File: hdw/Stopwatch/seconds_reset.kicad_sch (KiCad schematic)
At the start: 9 parts

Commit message: added more reset stuff
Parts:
- added C? (x4): 0.1uF, Capacitors_SMD:C_0603, symbol Custom_Library:C_Custom
- added R? (x4): 10k, Resistors_SMD:R_0603, symbol Custom_Library:R_Custom
- added U?: 74LVC1G97, Package_TO_SOT_SMD:SOT-363_SC-70-6, symbol Custom Library:74LVC1G97_Power_OR
- added U? (x3): 74LVC1G97, Package_TO_SOT_SMD:SOT-363_SC-70-6, symbol Custom Library:74LVC1G97_Power_AND
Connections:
- net +3.3V: now also U?.3 (VCC), U?.5 (VCC), U?.5 (VCC), U?.5 (VCC), U?.5 (VCC)
- net +3V3: now also C?.1, C?.1, C?.1, C?.1
- net GND: now also C?.2, C?.2, C?.2, C?.2, R?.2, R?.2, R?.2, R?.2, U?.1 (GND), U?.1 (GND), U?.1 (GND), U?.2 (GND), U?.2 (GND), U?.2 (GND), U?.2 (GND)
- net Stage01_SEG_G: now also U?.3
- net at R?.1, U?.4: now also U?.3
- net at R?.1, U?.4: now also U?.6 (x2)
- new net: R?.1, U?.4, U?.6 (x2)
- new net: R?.1, U?.3, U?.4
- new net Count_Reset: U?.1
- new net Seconds_Reset: R?.1, U?.4

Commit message: added some more junk
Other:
- company: (none) -> Drew Maatman
- title: (none) -> Stopwatch
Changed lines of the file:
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@@
 (kicad_sch (version 20230121) (generator eeschema)
   (paper "A")
+  (title_block
+    (title "Stopwatch")
+    (date "2024-01-11")
+    (rev "A")
+    (company "Drew Maatman")
+  )
   (junction (at 223.52 39.37) (diameter 0) (color 0 0 0 0)
   )

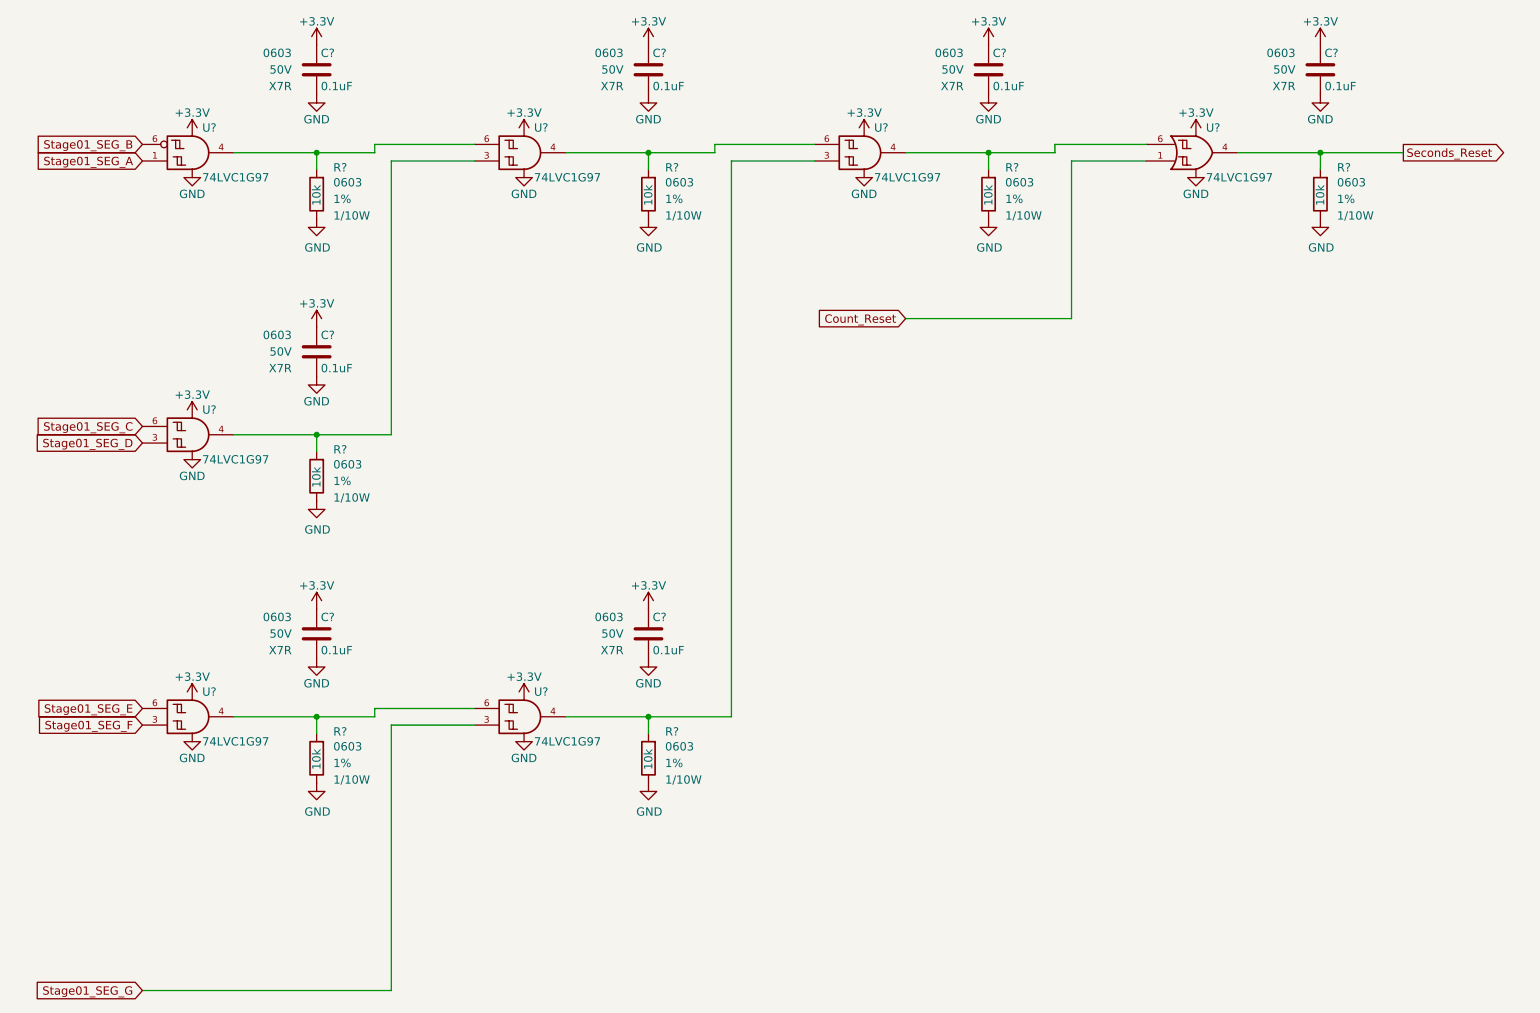
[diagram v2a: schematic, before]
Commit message: Assigned some digikey pns
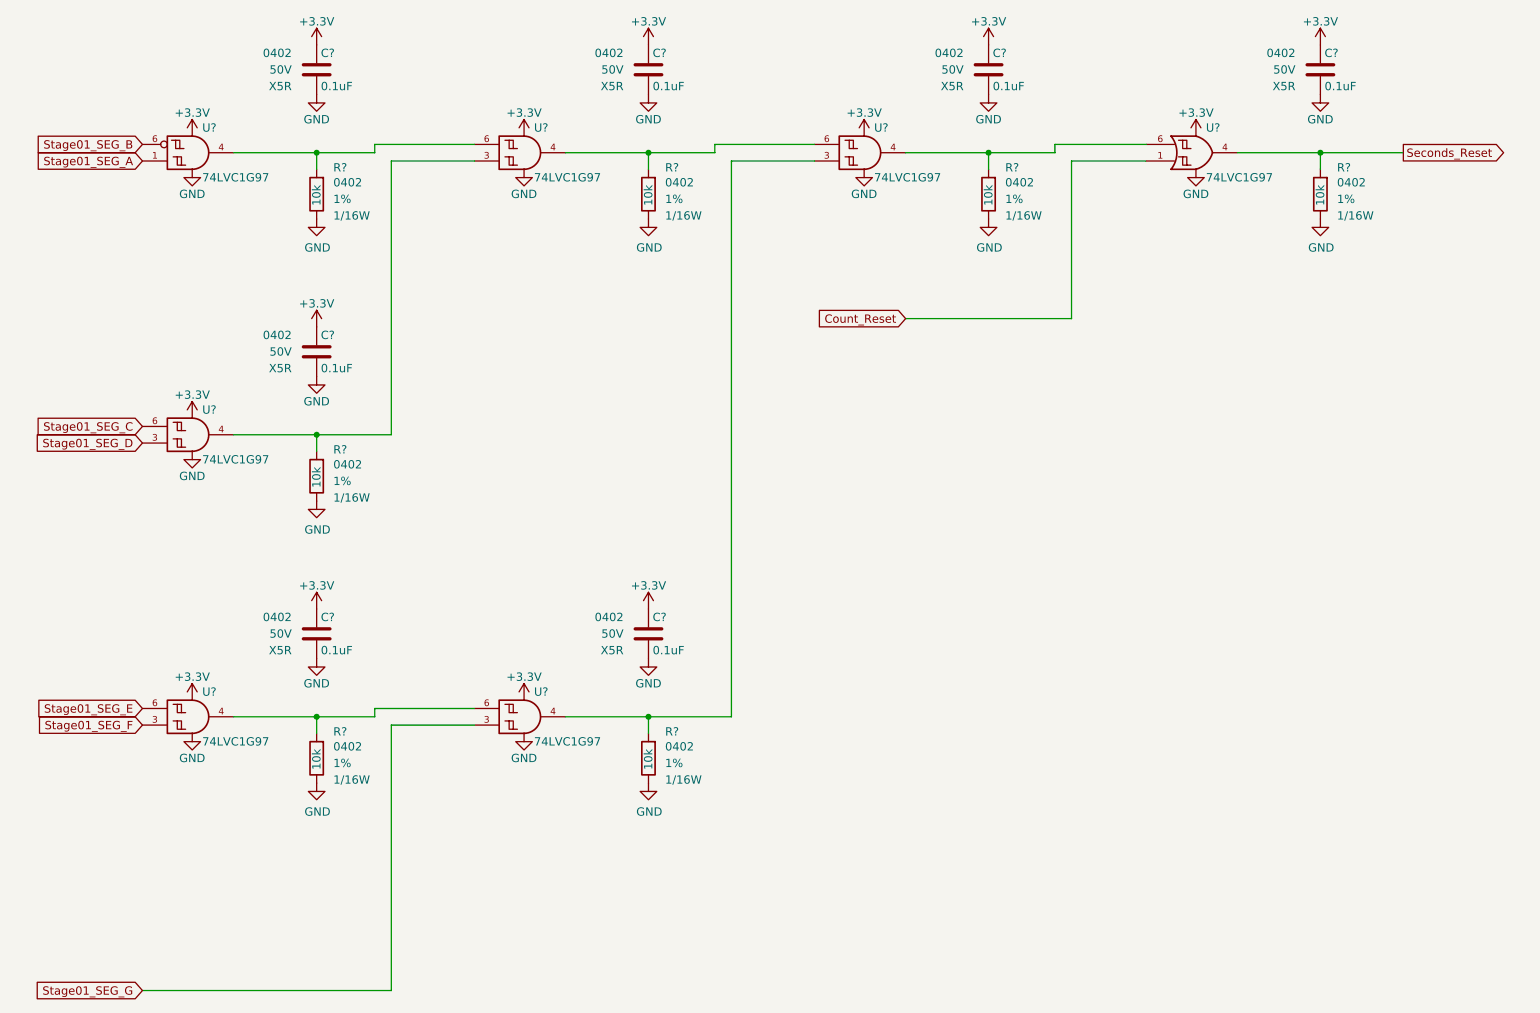
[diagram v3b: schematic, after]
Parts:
- C? (x7): footprint Capacitors_SMD:C_0603 -> Capacitors_SMD:C_0402; Dielectric X7R -> X5R; Digi-Key PN 311-1344-1-ND -> 490-10697-1-ND; display_footprint 0603 -> 0402
- R? (x7): footprint Resistors_SMD:R_0603 -> Resistors_SMD:R_0402; Digi-Key PN RMCF0603FT10K0CT-ND -> RMCF0402FT10K0CT-ND; Wattage 1/10W -> 1/16W; display_footprint 0603 -> 0402
- U? (x7): footprint Package_TO_SOT_SMD:SOT-363_SC-70-6 -> (none); Digi-Key PN (none) -> 296-29875-1-ND

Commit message: added proper power sequencing, discharge
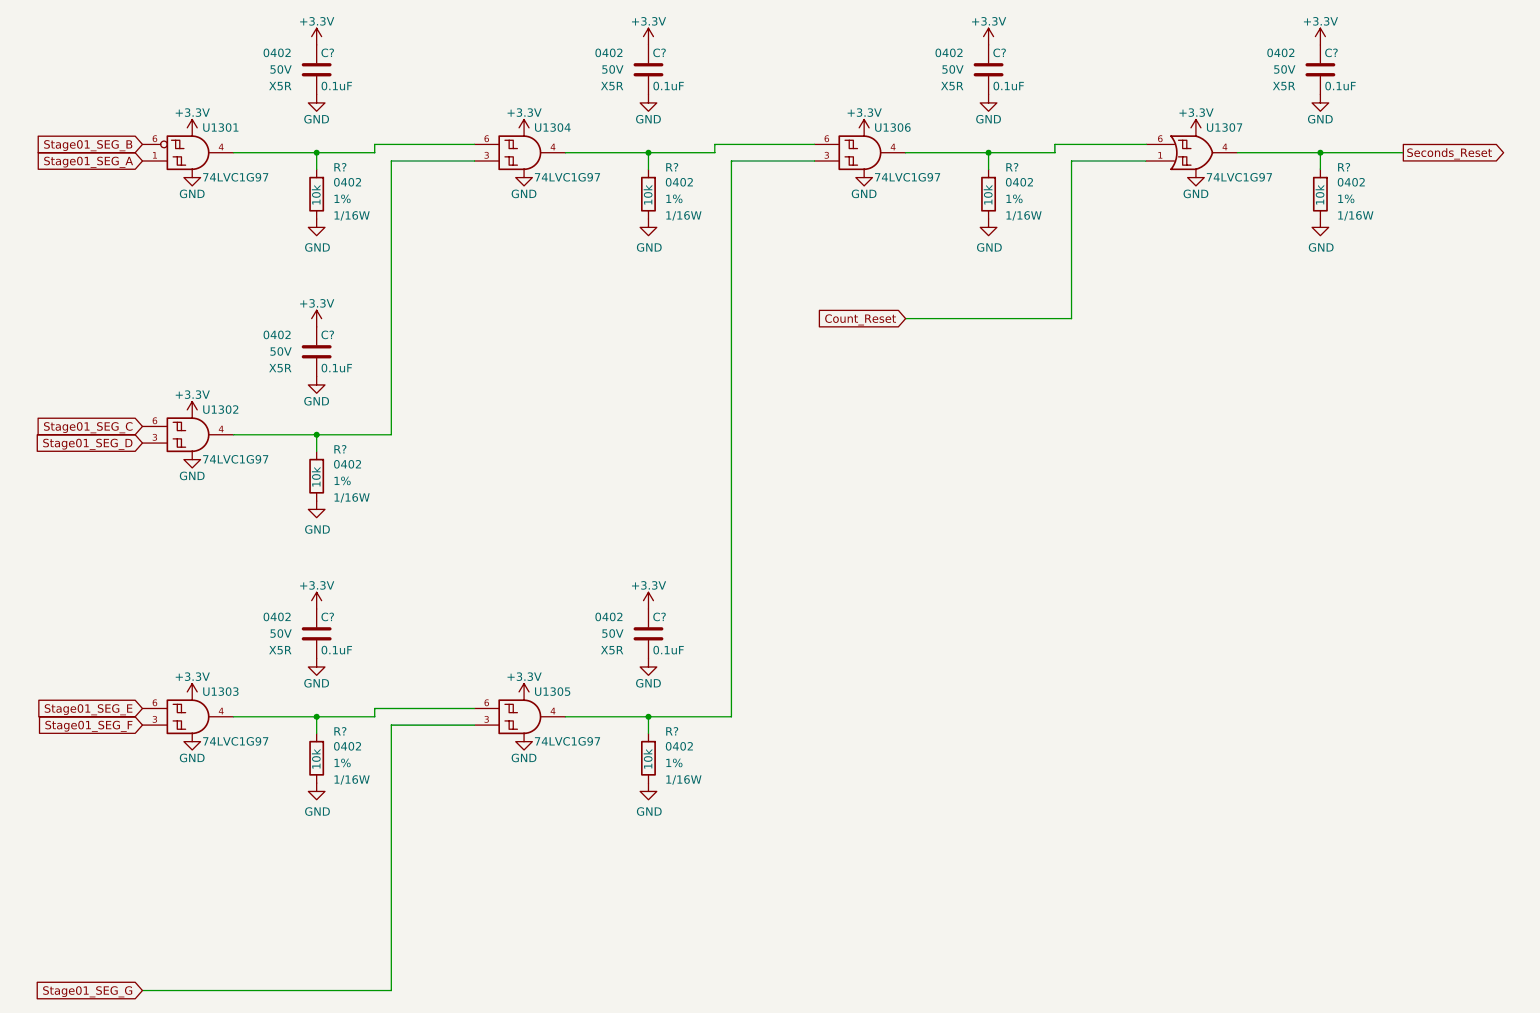
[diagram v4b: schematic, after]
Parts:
- U1301, U1302, U1303, U1304, U1305, U1306, U1307: renamed from U?; footprint (none) -> Package_SON:Fairchild_MicroPak2-6_1.0x1.0mm_P0.35mm

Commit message: lots and lots of routing
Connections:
- net +3V3 is gone; now on net +3.3V: C?.1, C?.1, C?.1, C?.1, C?.1, C?.1, C?.1
- net Stage01_SEG_A renamed Stage02_SEG_A
- net Stage01_SEG_B renamed Stage02_SEG_B
- net Stage01_SEG_C renamed Stage02_SEG_C
- net Stage01_SEG_D renamed Stage02_SEG_D
- net Stage01_SEG_E renamed Stage02_SEG_E
- net Stage01_SEG_F renamed Stage02_SEG_F
- net Stage01_SEG_G renamed Stage02_SEG_G
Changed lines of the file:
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@@
     (stroke (width 0) (type default))
   )
-  (global_label "Stage01_SEG_E" (shape input) (at 43.18 124.46 180) (fields_autoplaced)
+  (global_label "Stage02_SEG_E" (shape input) (at 43.18 124.46 180) (fields_autoplaced)
     (effects (font (size 1.27 1.27)) (justify right))
     (property "Intersheetrefs" "${INTERSHEET_REFS}" (at 26.4749 124.46 0)
@@
     )
   )
-  (global_label "Stage01_SEG_A" (shape input) (at 43.18 40.64 180) (fields_autoplaced)
+  (global_label "Stage02_SEG_A" (shape input) (at 43.18 40.64 180) (fields_autoplaced)
     (effects (font (size 1.27 1.27)) (justify right))
     (property "Intersheetrefs" "${INTERSHEET_REFS}" (at 26.5353 40.64 0)
@@
     )
   )
-  (global_label "Stage01_SEG_D" (shape input) (at 43.18 83.82 180) (fields_autoplaced)
+  (global_label "Stage02_SEG_D" (shape input) (at 43.18 83.82 180) (fields_autoplaced)
     (effects (font (size 1.27 1.27)) (justify right))
     (property "Intersheetrefs" "${INTERSHEET_REFS}" (at 26.3539 83.82 0)
@@
     )
   )
-  (global_label "Stage01_SEG_F" (shape input) (at 43.18 127 180) (fields_autoplaced)
+  (global_label "Stage02_SEG_F" (shape input) (at 43.18 127 180) (fields_autoplaced)
     (effects (font (size 1.27 1.27)) (justify right))
     (property "Intersheetrefs" "${INTERSHEET_REFS}" (at 26.5353 127 0)
@@
     )
   )
-  (global_label "Stage01_SEG_G" (shape input) (at 43.18 167.64 180) (fields_autoplaced)
+  (global_label "Stage02_SEG_G" (shape input) (at 43.18 167.64 180) (fields_autoplaced)
     (effects (font (size 1.27 1.27)) (justify right))
     (property "Intersheetrefs" "${INTERSHEET_REFS}" (at 26.3539 167.64 0)
@@
     )
   )
-  (global_label "Stage01_SEG_C" (shape input) (at 43.18 81.28 180) (fields_autoplaced)
+  (global_label "Stage02_SEG_C" (shape input) (at 43.18 81.28 180) (fields_autoplaced)
     (effects (font (size 1.27 1.27)) (justify right))
     (property "Intersheetrefs" "${INTERSHEET_REFS}" (at 26.3539 81.28 0)
@@
     )
   )
-  (global_label "Stage01_SEG_B" (shape input) (at 43.18 38.1 180) (fields_autoplaced)
+  (global_label "Stage02_SEG_B" (shape input) (at 43.18 38.1 180) (fields_autoplaced)
     (effects (font (size 1.27 1.27)) (justify right))
     (property "Intersheetrefs" "${INTERSHEET_REFS}" (at 26.3539 38.1 0)
@@
     )
   )
-  (symbol (lib_id "Incrementor-rescue:+3.3V-power") (at 223.52 22.86 0) (unit 1)
+  (symbol (lib_id "power:+3.3V") (at 223.52 22.86 0) (unit 1)
     (in_bom yes) (on_board yes) (dnp no)
     (property "Reference" "#PWR?" (at 223.52 26.67 0)
@@
     )
   )
-  (symbol (lib_id "Incrementor-rescue:+3.3V-power") (at 69.85 66.04 0) (unit 1)
+  (symbol (lib_id "power:+3.3V") (at 69.85 66.04 0) (unit 1)
     (in_bom yes) (on_board yes) (dnp no)
     (property "Reference" "#PWR?" (at 69.85 69.85 0)
@@
     )
   )
-  (symbol (lib_id "Incrementor-rescue:+3.3V-power") (at 69.85 109.22 0) (unit 1)
+  (symbol (lib_id "power:+3.3V") (at 69.85 109.22 0) (unit 1)
     (in_bom yes) (on_board yes) (dnp no)
     (property "Reference" "#PWR?" (at 69.85 113.03 0)
@@
     )
   )
-  (symbol (lib_id "Incrementor-rescue:+3.3V-power") (at 172.72 22.86 0) (unit 1)
+  (symbol (lib_id "power:+3.3V") (at 172.72 22.86 0) (unit 1)
     (in_bom yes) (on_board yes) (dnp no)
     (property "Reference" "#PWR?" (at 172.72 26.67 0)
@@
     )
   )
-  (symbol (lib_id "Incrementor-rescue:+3.3V-power") (at 120.65 22.86 0) (unit 1)
+  (symbol (lib_id "power:+3.3V") (at 120.65 22.86 0) (unit 1)
     (in_bom yes) (on_board yes) (dnp no)
     (property "Reference" "#PWR?" (at 120.65 26.67 0)
@@
     )
   )
-  (symbol (lib_id "Incrementor-rescue:+3.3V-power") (at 120.65 109.22 0) (unit 1)
+  (symbol (lib_id "power:+3.3V") (at 120.65 109.22 0) (unit 1)
     (in_bom yes) (on_board yes) (dnp no)
     (property "Reference" "#PWR?" (at 120.65 113.03 0)
@@
     )
   )
-  (symbol (lib_id "Incrementor-rescue:+3.3V-power") (at 69.85 22.86 0) (unit 1)
+  (symbol (lib_id "power:+3.3V") (at 69.85 22.86 0) (unit 1)
     (in_bom yes) (on_board yes) (dnp no)
     (property "Reference" "#PWR?" (at 69.85 26.67 0)

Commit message: got no unconnects to 0
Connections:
- net Stage02_SEG_A: now also U1302.3; no longer U1301.1
- net Stage02_SEG_D: now also U1301.1; no longer U1302.3
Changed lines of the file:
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@@
     )
   )
-  (global_label "Stage02_SEG_A" (shape input) (at 43.18 40.64 180) (fields_autoplaced)
+  (global_label "Stage02_SEG_A" (shape input) (at 43.18 83.82 180) (fields_autoplaced)
     (effects (font (size 1.27 1.27)) (justify right))
-    (property "Intersheetrefs" "${INTERSHEET_REFS}" (at 26.5353 40.64 0)
+    (property "Intersheetrefs" "${INTERSHEET_REFS}" (at 26.5353 83.82 0)
       (effects (font (size 1.27 1.27)) (justify right) hide)
     )
   )
-  (global_label "Stage02_SEG_D" (shape input) (at 43.18 83.82 180) (fields_autoplaced)
+  (global_label "Stage02_SEG_D" (shape input) (at 43.18 40.64 180) (fields_autoplaced)
     (effects (font (size 1.27 1.27)) (justify right))
-    (property "Intersheetrefs" "${INTERSHEET_REFS}" (at 26.3539 83.82 0)
+    (property "Intersheetrefs" "${INTERSHEET_REFS}" (at 26.3539 40.64 0)
       (effects (font (size 1.27 1.27)) (justify right) hide)
     )
